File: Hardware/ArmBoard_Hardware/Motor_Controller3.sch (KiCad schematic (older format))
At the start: 13 parts

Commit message: added missing lables to connectors
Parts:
- MC3: symbol MRDT_ICs:VNH5019A_E -> ArmBoard_Hardware-rescue:VNH5019A_E-MRDT_ICs
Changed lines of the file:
@@
 IN_A_3
 $Comp
-L MRDT_ICs:VNH5019A_E U?
+L ArmBoard_Hardware-rescue:VNH5019A_E-MRDT_ICs U?
 U 1 1 62E6C905
 P 4925 4600

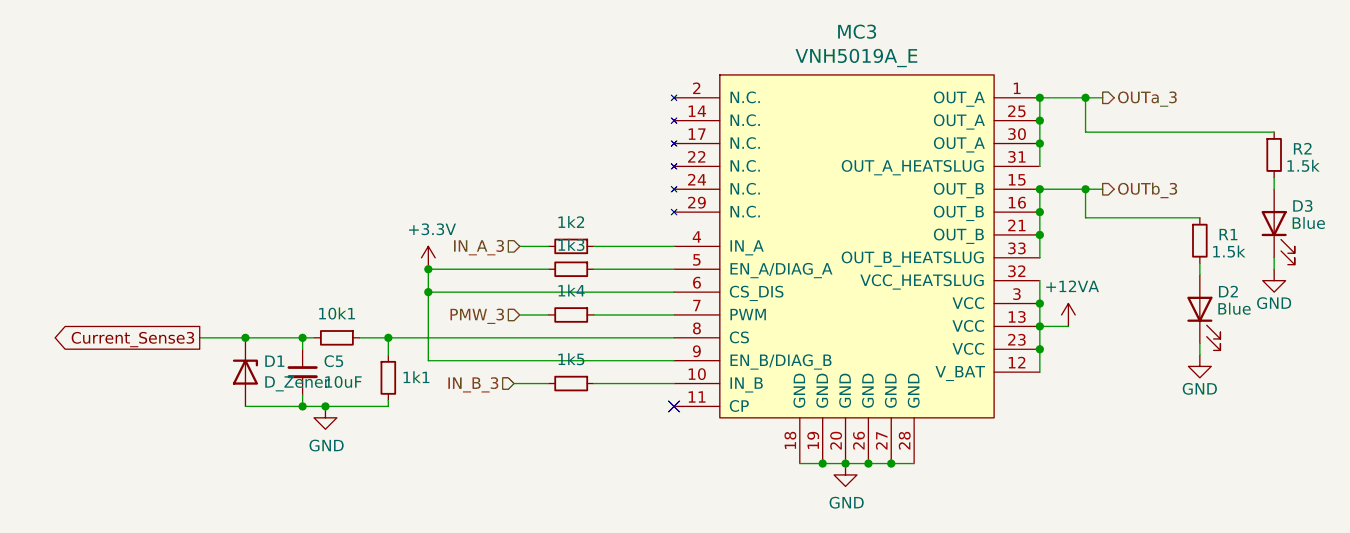
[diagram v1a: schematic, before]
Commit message: schematic changes, encoder changes, led changes
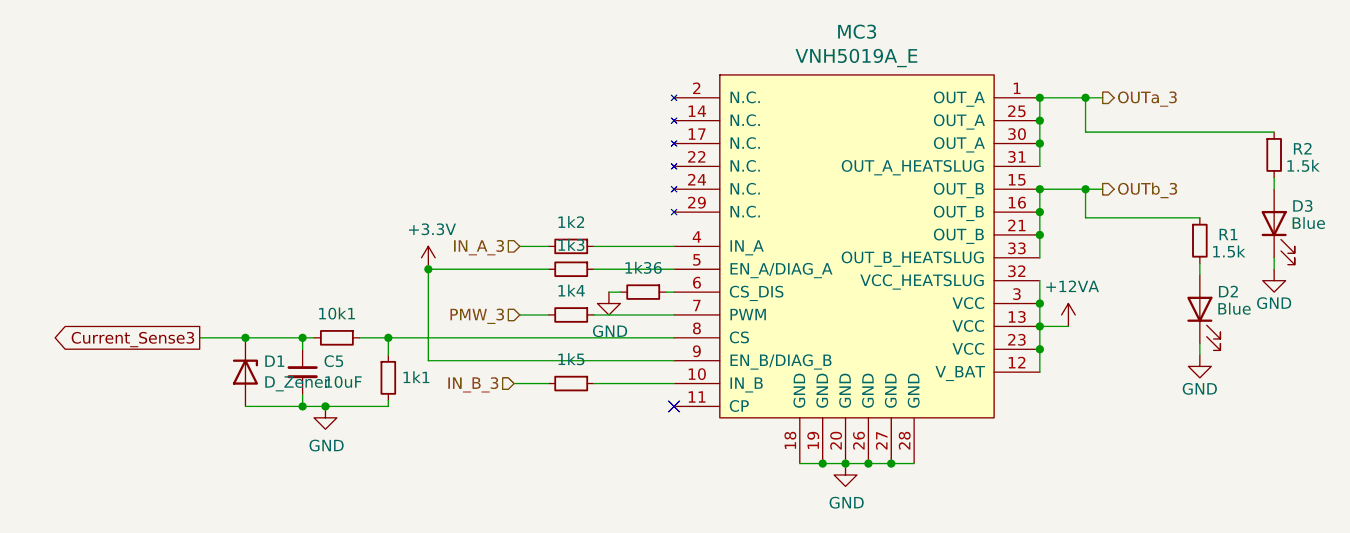
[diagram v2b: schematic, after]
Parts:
- added 1k36: R_Small, Resistor_SMD:R_0603_1608Metric_Pad0.98x0.95mm_HandSolder, symbol Device:R_Small
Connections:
- net +3V3: no longer MC3.6 (CS_DIS)
- net GND: now also 1k36.2
- new net: 1k36.1, MC3.6 (CS_DIS)
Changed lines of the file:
@@
 Wire Wire Line
 	4175 4150 4050 4150
-Wire Wire Line
-	4725 4050 3650 4050
-Wire Wire Line
-	3650 4050 3650 3950
 Connection ~ 3650 3950
 Wire Wire Line
 	4725 4350 3650 4350
-Wire Wire Line
-	3650 4350 3650 4050
-Connection ~ 3650 4050
 Wire Wire Line
 	4725 4250 3475 4250
@@
 Text HLabel 6600 3600 2    50   Output ~ 0
 OUTb_3
+Wire Wire Line
+	3650 3950 3650 4350
+$Comp
+L power:GND #PWR?
+U 1 1 62927260
+P 4440 4050
+AR Path="/63845F20/62927260" Ref="#PWR?"  Part="1"
+AR Path="/628CE14B/62927260" Ref="#PWR?"  Part="1"
+AR Path="/6297969A/62927260" Ref="#PWR?"  Part="1"
+AR Path="/629F46F6/62927260" Ref="#PWR?"  Part="1"
+AR Path="/629F46FD/62927260" Ref="#PWR?"  Part="1"
+AR Path="/62A5CC3B/62927260" Ref="#PWR?"  Part="1"
+AR Path="/62A5CC46/62927260" Ref="#PWR?"  Part="1"
+AR Path="/62AF9C52/62927260" Ref="#PWR01"  Part="1"
+AR Path="/62D2CE1B/62927260" Ref="#PWR?"  Part="1"
+F 0 "#PWR01" H 4440 3800 50  0001 C CNN
+F 1 "GND" H 4445 3877 50  0000 C CNN
+F 2 "" H 4440 4050 50  0001 C CNN
+F 3 "" H 4440 4050 50  0001 C CNN
+	1    4440 4050
+	1    0    0    -1
+$EndComp
+$Comp
+L Device:R_Small 1k?
+U 1 1 62927266
+P 4590 4050
+AR Path="/63845F20/62927266" Ref="1k?"  Part="1"
+AR Path="/628CE14B/62927266" Ref="1k?"  Part="1"
+AR Path="/6297969A/62927266" Ref="1k?"  Part="1"
+AR Path="/629F46F6/62927266" Ref="1k?"  Part="1"
+AR Path="/629F46FD/62927266" Ref="1k?"  Part="1"
+AR Path="/62A5CC3B/62927266" Ref="1k?"  Part="1"
+AR Path="/62A5CC46/62927266" Ref="1k?"  Part="1"
+AR Path="/62AF9C52/62927266" Ref="1k36"  Part="1"
+AR Path="/62C19165/62927266" Ref="1k?"  Part="1"
+AR Path="/62CA8FD7/62927266" Ref="1k?"  Part="1"
+AR Path="/62CBA1AC/62927266" Ref="1k?"  Part="1"
+AR Path="/62CCE879/62927266" Ref="1k?"  Part="1"
+AR Path="/62CE0B38/62927266" Ref="1k?"  Part="1"
+AR Path="/62CF1227/62927266" Ref="1k?"  Part="1"
+AR Path="/62D0C672/62927266" Ref="1k?"  Part="1"
+AR Path="/62D1BEB1/62927266" Ref="1k?"  Part="1"
+AR Path="/62D2CE1B/62927266" Ref="1k?"  Part="1"
+AR Path="/62D3BCB9/62927266" Ref="1k?"  Part="1"
+AR Path="/62D4BAA1/62927266" Ref="1k?"  Part="1"
+F 0 "1k36" V 4486 4050 50  0000 C CNN
+F 1 "R_Small" V 4485 4050 50  0001 C CNN
+F 2 "Resistor_SMD:R_0603_1608Metric_Pad0.98x0.95mm_HandSolder" H 4590 4050 50  0001 C CNN
+F 3 "~" H 4590 4050 50  0001 C CNN
+	1    4590 4050
+	0    1    1    0
+$EndComp
+Wire Wire Line
+	4440 4050 4490 4050
+Wire Wire Line
+	4690 4050 4725 4050
 $EndSCHEMATC

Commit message: gerbs added and zipped
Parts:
- MC3: symbol ArmBoard_Hardware-rescue:VNH5019A_E-MRDT_ICs -> MRDT_ICs:VNH5019A_E
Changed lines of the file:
@@
 IN_A_3
 $Comp
-L ArmBoard_Hardware-rescue:VNH5019A_E-MRDT_ICs U?
+L MRDT_ICs:VNH5019A_E U?
 U 1 1 62E6C905
 P 4925 4600
